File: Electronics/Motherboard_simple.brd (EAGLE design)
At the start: 69.8 x 54.6 mm, 23 parts

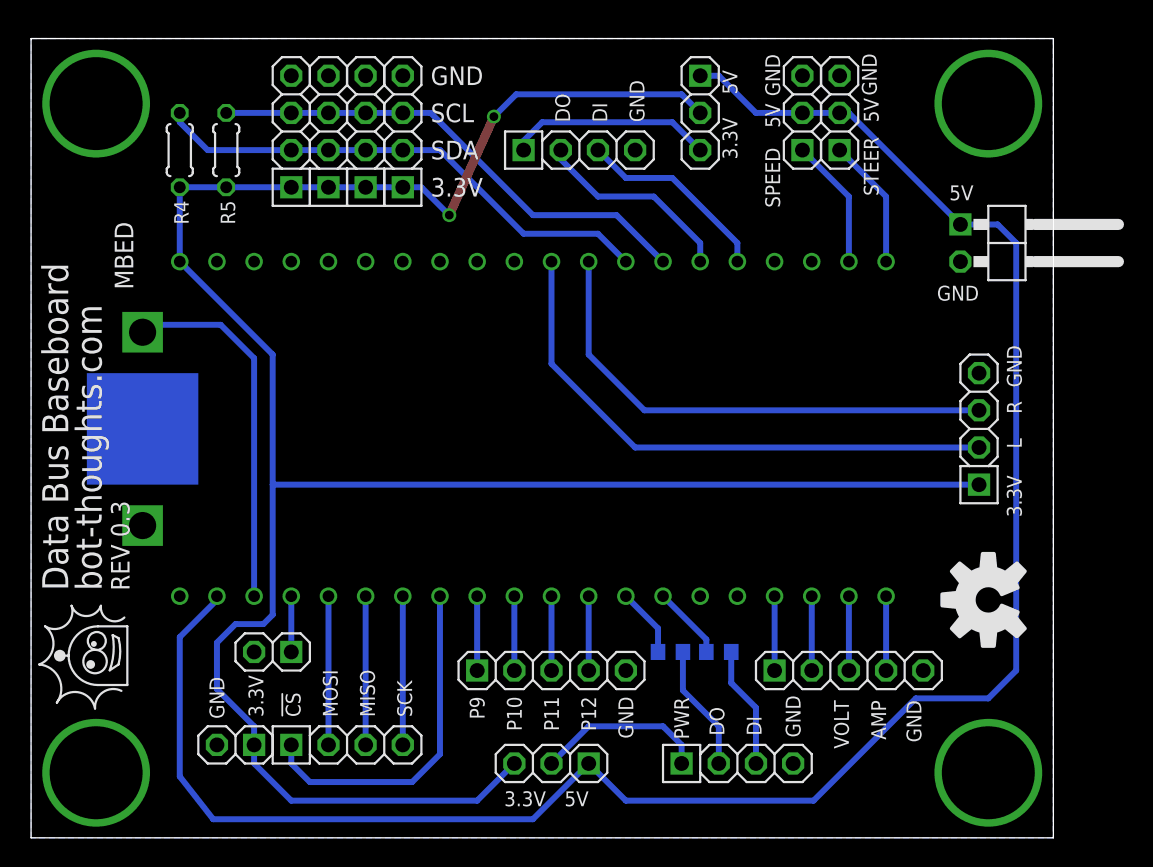
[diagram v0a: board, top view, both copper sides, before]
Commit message: Initial Revision for microSD breakout, revised microsd pin header for motherboard, other minor tweaks to motherboard.
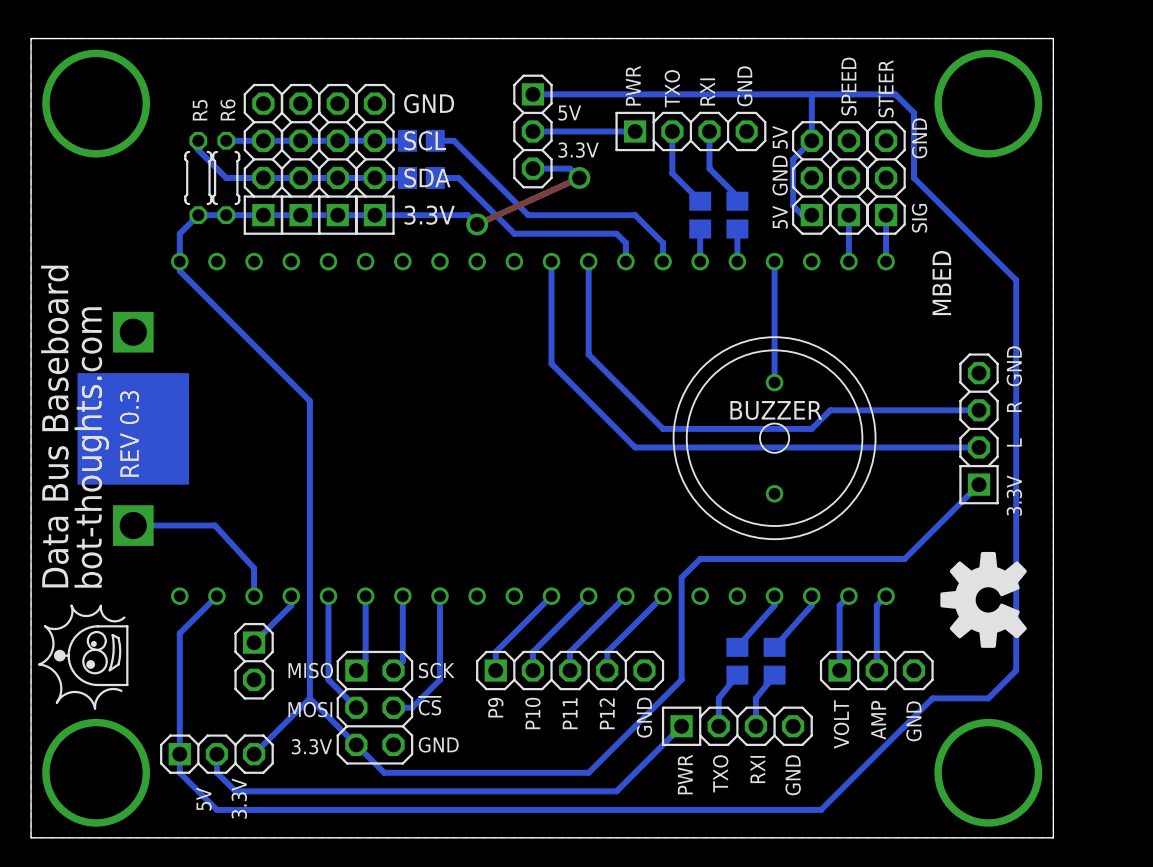
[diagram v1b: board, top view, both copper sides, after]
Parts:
- removed JP1: PWR, pinhead-2:1X02/90-S
- removed JP10: microSD 3.3V, pinhead-2:1X04-S
- removed JP5: PWR, pinhead-2:1X02-S
- added BUZZER: 1438-TWT-R, mes_buzzers:BUZZER_14MM_PTH
- added JP19: POWER, pinhead-2:1X03-S
- added R3, R7, R8: 220, rcl:R0805
- added R6: 2.2K, rcl:0204/5
- added SV1: microSD, pinhead-2:2X03
- JP16: value PWR -> PSEL3
- JP17: value ANALOG -> VASENSE; device pinhead-2:1X05-S -> pinhead-2:1X03-S
- JP2: value SER2 -> UART1
- JP3: value PWR -> PSEL1
- JP6: value SER1 -> UART3
- R1, R2: device rcl:R0603 -> rcl:R0805
- R4: value 2.2K -> 220; device rcl:0204/5 -> rcl:R0805
- moved R4 38.4 mm to (48.3, 42.5), flipped to the bottom, turned to 90 degrees
- moved JP16 22.9 mm to (12.7, 5.71), turned to 0 degrees
- moved JP3 11.5 mm to (34.3, 48.3)
- moved JP2 7.73 mm to (45.1, 48.3)
- moved JP8 5.46 mm to (55.9, 45.1)
- moved JP9 5.46 mm to (58.4, 45.1)
- moved R1 4.62 mm to (48.3, 12.1), turned to 270 degrees
- moved R2 3.86 mm to (50.8, 12.1), turned to 270 degrees
- moved JP11 2.69 mm to (18.4, 46.4)
- moved JP13 2.69 mm to (15.9, 46.4)
- moved JP14 2.69 mm to (21.0, 46.4)
- moved R5 2.69 mm to (11.4, 45.1)
- moved JP12 2.69 mm to (23.5, 46.4)
- moved JP6 2.54 mm to (48.3, 7.62)
- moved JP17 1.90 mm to (57.8, 11.4)
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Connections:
- removed net RX1: MBED.P$14, R2.1
- removed net RX2: JP2.3, MBED.P$25
- removed net TX1: MBED.P$13, R1.1
- removed net TX2: JP2.2, MBED.P$26
- new net N$12: BUZZER.P$1, MBED.P$24
- new net N$13: MBED.P$28, R7.2
- new net N$14: MBED.P$27, R8.2
- new net RXD1: MBED.P$25, R4.1
- new net RXD3: MBED.P$18, R2.1
- new net TXD1: MBED.P$26, R3.1
- new net TXD3: MBED.P$17, R1.1
- net !CS1: now also SV1.4; no longer JP10.1
- net +3V3: now also JP3.3, R6.2, SV1.5; no longer JP3.2, JP5.1, R4.2
- net +5V: now also JP19.1, JP19.3; no longer JP1.1, JP8.2, JP9.2
- net AMP: now also JP17.2; no longer JP17.4
- net GND: now also BUZZER.P$2, JP17.3, JP19.2, SV1.6; no longer JP1.2, JP17.5, JP5.2
- net MISO1: now also SV1.1; no longer JP10.3
- net MOSI1: now also SV1.3; no longer JP10.2
- net N$10: now also JP2.3, R4.2; no longer JP17.1, MBED.P$17
- net N$11: now also JP3.2; no longer JP3.3
- net N$4: now also MBED.P$11; no longer MBED.P$9
- net N$5: now also MBED.P$12; no longer MBED.P$10
- net N$6: now also JP17.1; no longer JP17.3
- net N$7: now also MBED.P$13; no longer MBED.P$11
- net N$8: now also MBED.P$14; no longer MBED.P$12
- net N$9: now also JP2.2, R3.2; no longer JP17.2, MBED.P$18
- net SCK1: now also SV1.2; no longer JP10.4
- net SCL: now also R6.1, R8.1; no longer MBED.P$27, R5.1
- net SDA: now also R5.1, R7.1; no longer MBED.P$28, R4.1
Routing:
- net N$3: track 11.7 -> 35.4 mm
- net +3V3: track 155.7 -> 133.1 mm
- net SCL: track 34.1 -> 12.7 mm
- net N$14: track 0.00 -> 19.7 mm
- net SDA: track 35.1 -> 15.7 mm
- net +5V: track 133.8 -> 152.5 mm
- net N$13: track 0.00 -> 16.1 mm
- net !CS1: track 23.5 -> 9.68 mm
- net TX2: track 13.8 -> 0.00 mm
- net VB: track 25.0 -> 11.4 mm
- net RX2: track 13.4 -> 0.00 mm
- net N$12: track 0.00 -> 8.26 mm
- net N$11: track 14.0 -> 6.98 mm
- net STEER: track 8.94 -> 3.18 mm
- net SPEED: track 8.94 -> 3.18 mm
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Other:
- board text added: "RXI"
- board text added: "SIG"
- board text added: "TXO"
- board text added: "Yes, this is backwards; fix when mounting"
- board text removed: "DI"
- board text removed: "DO"

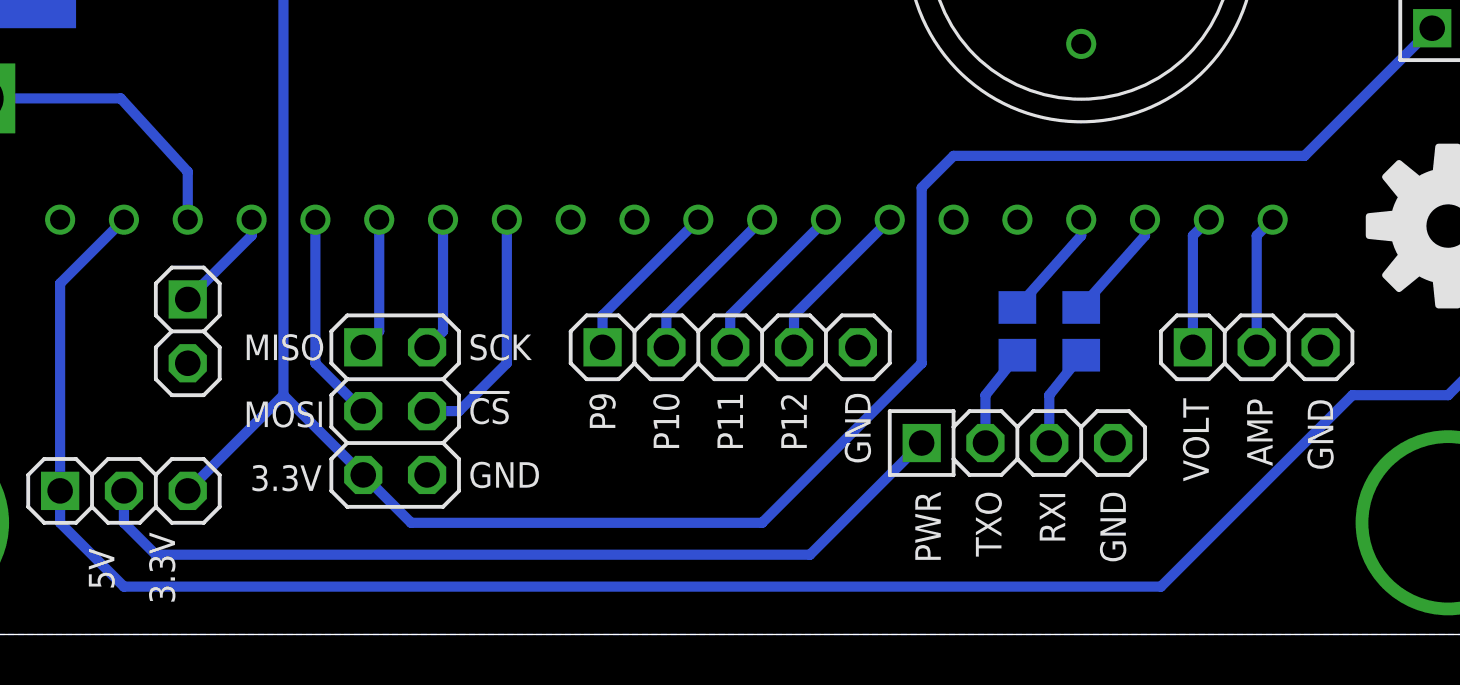
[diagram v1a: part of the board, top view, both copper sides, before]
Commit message: Tweaks to make room for SPI2
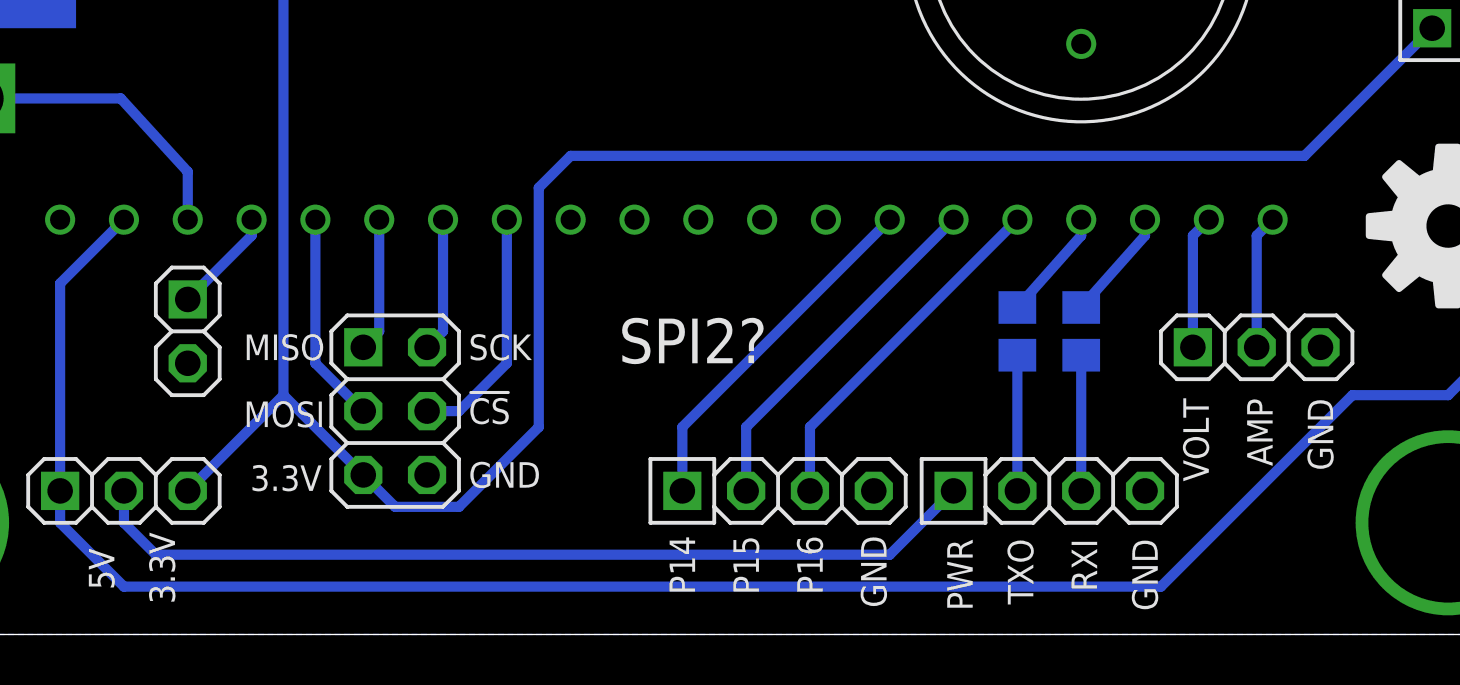
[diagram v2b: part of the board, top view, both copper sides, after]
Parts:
- removed JP7: BUTTONS, pinhead-2:1X05-S
- added JP1: BUTTONS, pinhead-2:1X04-S
- moved JP6 2.29 mm to (49.5, 5.71)
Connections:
- removed net N$4: JP7.1, MBED.P$11
- new net !CS2: MBED.P$10
- new net MISO2: MBED.P$12
- new net MOSI2: MBED.P$11
- new net SCK2: MBED.P$13
- net GND: now also JP1.4; no longer JP7.5
- net N$5: now also JP1.1, MBED.P$14; no longer JP7.2, MBED.P$12
- net N$7: now also JP1.2, MBED.P$15; no longer JP7.3, MBED.P$13
- net N$8: now also JP1.3, MBED.P$16; no longer JP7.4, MBED.P$14
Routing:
- net N$5: track 6.66 -> 14.2 mm
- net N$8: track 6.66 -> 14.2 mm
- net N$7: track 6.66 -> 14.2 mm
- net N$4: track 6.66 -> 0.00 mm
- net N$2: track 3.94 -> 5.40 mm
- net N$1: track 3.94 -> 5.40 mm
- net +3V3: track 133.1 -> 134.1 mm
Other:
- board text added: "P14"
- board text added: "P15"
- board text added: "P16"
- board text added: "SPI2?"
- board text removed: "P10"
- board text removed: "P11"
- board text removed: "P12"
- board text removed: "P9"

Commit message: Minor updates and tweaks
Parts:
- removed JP16: PSEL3, pinhead-2:1X03-S
- removed JP3: PSEL1, pinhead-2:1X03-S
- added JP10: UART2, pinhead-2:1X04-S
- added JP5: I2C, pinhead-2:1X04-S
- added JP7: PPS, pinhead-2:1X01-S
- added R10, R9: 220, rcl:R0805
- BAT1: device SparkFun:BATTCON_12MM_PTH -> SparkFun:BATTCON_12MM
- JP1: device pinhead-2:1X04-S -> pinhead-2:2X02
- JP17: value VASENSE -> VA
- moved JP1 8.82 mm to (46.4, 10.2)
- moved R2 3.59 mm to (53.3, 9.53)
- moved R1 3.59 mm to (50.8, 9.53)
- moved JP2 3.18 mm to (41.9, 48.3)
- moved R6 1.91 mm to (11.4, 45.1)
- moved R5 1.90 mm to (9.53, 45.1)
- moved JP17 1.27 mm to (57.8, 12.7)
- moved JP11 0.64 mm to (19.1, 46.4)
- moved JP13 0.64 mm to (16.5, 46.4)
- moved JP14 0.64 mm to (21.6, 46.4)
- moved JP12 0.63 mm to (24.1, 46.4)
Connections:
- removed net !CS2: MBED.P$10
- removed net MISO2: MBED.P$12
- removed net MOSI2: MBED.P$11
- removed net N$11: JP2.1, JP3.2
- removed net N$3: JP16.2, JP6.1
- removed net SCK2: MBED.P$13
- new net N$16: JP10.2, R9.2
- new net N$17: JP10.3, R10.2
- new net PPS: JP7.1, MBED.P$23
- new net RXD2: MBED.P$10, R10.1
- new net TXD2: MBED.P$9, R9.1
- net +3V3: now also JP10.1, JP2.1, JP5.1, JP6.1; no longer JP16.3, JP3.3
- net +5V: no longer JP16.1, JP3.1
- net GND: now also JP1.1, JP10.4, JP5.4; no longer JP1.4
- net N$5: now also JP1.2; no longer JP1.1
- net N$7: now also JP1.4; no longer JP1.2
- net SCL: now also JP5.3
- net SDA: now also JP5.2
- net VB: now also BAT1.PWR@1; no longer BAT1.VCC@1
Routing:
- net N$3: track 35.9 -> 0.00 mm
- net +5V: track 152.5 -> 124.3 mm
- net PPS: track 0.00 -> 11.0 mm
- net N$16: track 0.00 -> 9.63 mm
- net N$5: track 14.2 -> 5.87 mm
- net N$7: track 14.2 -> 5.87 mm
- net +3V3: track 134.1 -> 141.5 mm
- net N$11: track 6.98 -> 0.00 mm
- net N$8: track 14.2 -> 8.41 mm
- net N$17: track 0.00 -> 4.92 mm
- net TXD2: track 0.00 -> 2.23 mm
- net RXD2: track 0.00 -> 2.23 mm
- net SCL: track 12.7 -> 14.6 mm
- net N$1: track 5.40 -> 3.83 mm
- net TXD3: track 4.46 -> 6.04 mm
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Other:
- board text removed: "PWR"
- board text removed: "SPI2?"

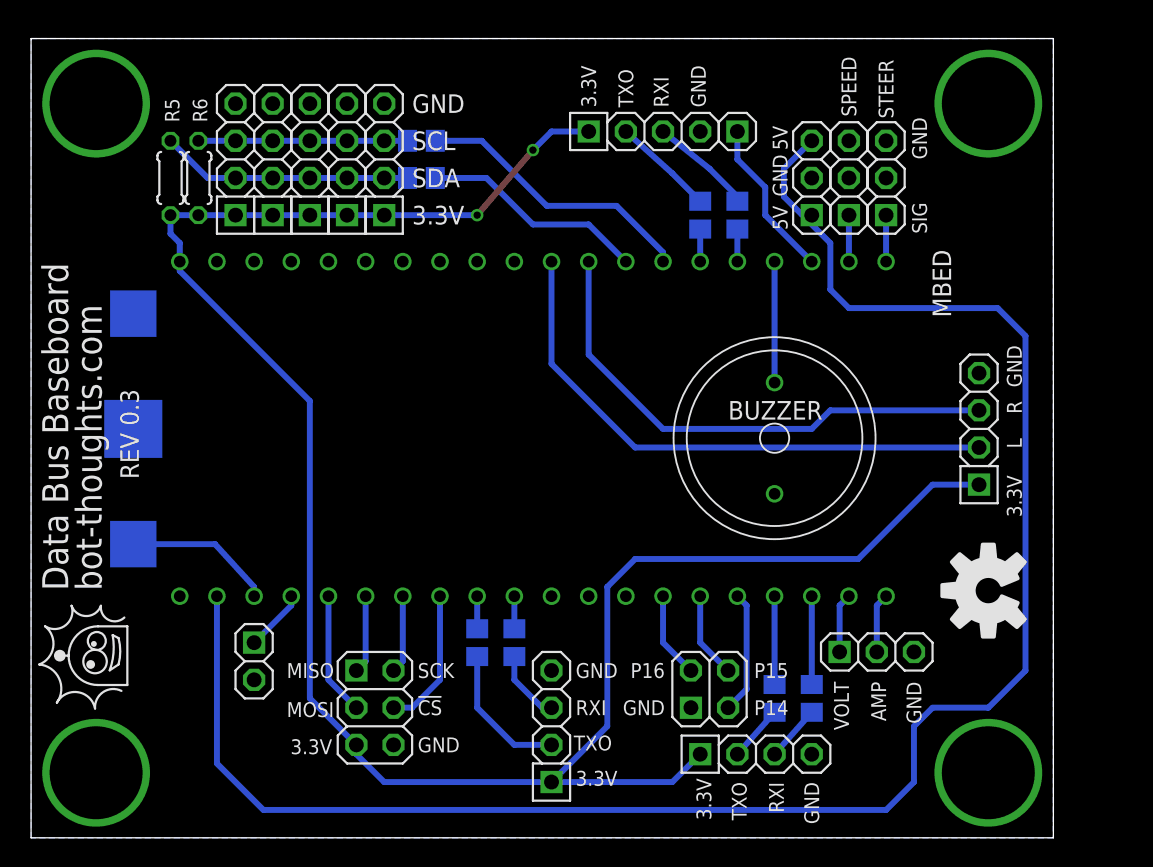
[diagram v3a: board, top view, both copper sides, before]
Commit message: Removed battery, added microSD, more room now, yay.
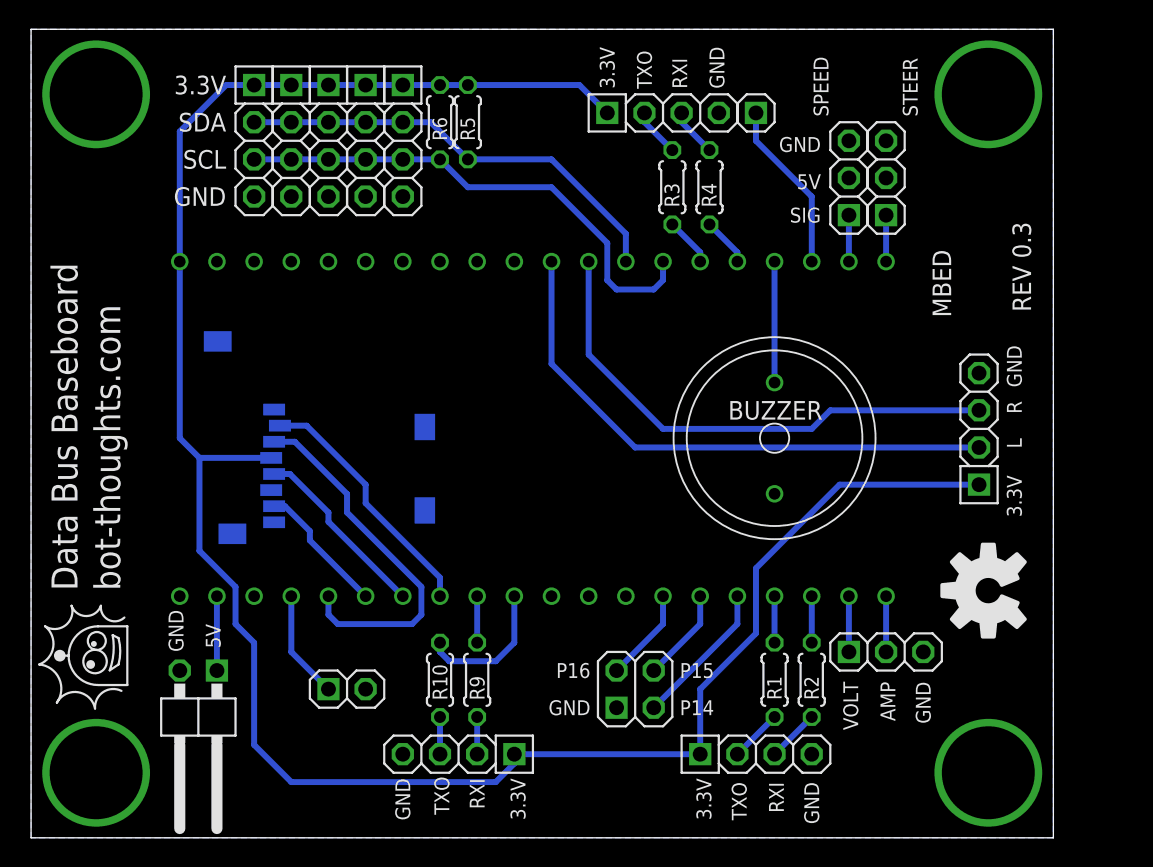
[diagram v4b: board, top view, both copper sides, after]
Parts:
- removed BAT1: (no value), SparkFun:BATTCON_12MM
- removed JP19: POWER, pinhead-2:1X03-S
- removed R7, R8: 220, rcl:R0805
- removed SV1: microSD, pinhead-2:2X03
- added JP3: POWER, pinhead-2:1X02/90-S
- added U2: USD-SOCKETNEW, SparkFun:MICRO-SD-SOCKET-PP
- R1, R10, R2, R3, R4, R9: device rcl:R0805 -> rcl:0204/5
- moved R5 20.7 mm to (29.8, 48.9), turned to 90 degrees
- moved R6 16.9 mm to (27.9, 48.9), turned to 90 degrees
- moved JP5 11.5 mm to (25.4, 47.6), turned to 270 degrees
- moved JP12 8.98 mm to (15.2, 47.6), turned to 270 degrees
- moved JP10 6.63 mm to (29.2, 5.71), turned to 180 degrees
- moved JP4 6.63 mm to (21.6, 10.2), turned to 0 degrees
- moved JP13 6.48 mm to (22.9, 47.6), turned to 270 degrees
- moved R10 5.68 mm to (27.9, 10.8), flipped to the top
- moved JP1 5.08 mm to (41.3, 10.2)
- moved JP14 4.02 mm to (17.8, 47.6), turned to 270 degrees
- moved R3 2.69 mm to (43.8, 44.5), flipped to the top
- moved R4 2.69 mm to (46.4, 44.5), flipped to the top
- moved R9 2.54 mm to (30.5, 10.8), flipped to the top
- moved JP2 1.80 mm to (43.2, 49.5)
- moved JP7 1.80 mm to (49.5, 49.5)
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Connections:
- removed net N$13: MBED.P$28, R7.2
- removed net N$14: MBED.P$27, R8.2
- net !CS1: now also U2.2; no longer SV1.4
- net +3V3: now also U2.4; no longer SV1.5
- net +5V: now also JP3.1; no longer JP19.1, JP19.3
- net GND: now also JP3.2, U2.6, U2.GND1, U2.GND3; no longer BAT1.GND, JP19.2, SV1.6
- net MISO1: now also U2.7; no longer SV1.1
- net MOSI1: now also U2.3; no longer SV1.3
- net SCK1: now also U2.5; no longer SV1.2
- net SCL: now also MBED.P$27; no longer R8.1
- net SDA: now also MBED.P$28; no longer R7.1
- net VB: no longer BAT1.PWR@1
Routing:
- net +5V: track 124.3 -> 5.08 mm
- net SCL: track 14.6 -> 34.6 mm
- net N$14: track 19.4 -> 0.00 mm
- net MOSI1: track 8.41 -> 25.0 mm
- net N$13: track 15.4 -> 0.00 mm
- net SDA: track 17.2 -> 30.5 mm
- net VB: track 10.2 -> 0.00 mm
- net !CS1: track 9.68 -> 17.2 mm
- net RXD2: track 2.23 -> 9.68 mm
- net SCK1: track 5.34 -> 12.6 mm
- net N$16: track 9.63 -> 2.54 mm
- net MISO1: track 5.34 -> 9.17 mm
- net N$10: track 7.08 -> 3.33 mm
- net N$9: track 6.97 -> 3.33 mm
- net +3V3: track 141.5 -> 144.8 mm, vias 2 -> 0
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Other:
- board size 69.8 x 54.6 mm -> 69.8 x 55.2 mm
- board text removed: "!CS"
- board text removed: "MISO"
- board text removed: "MOSI"
- board text removed: "SCK"
